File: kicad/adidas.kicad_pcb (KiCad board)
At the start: 2 copper layers, 152.7 x 107.2 mm, 7 parts

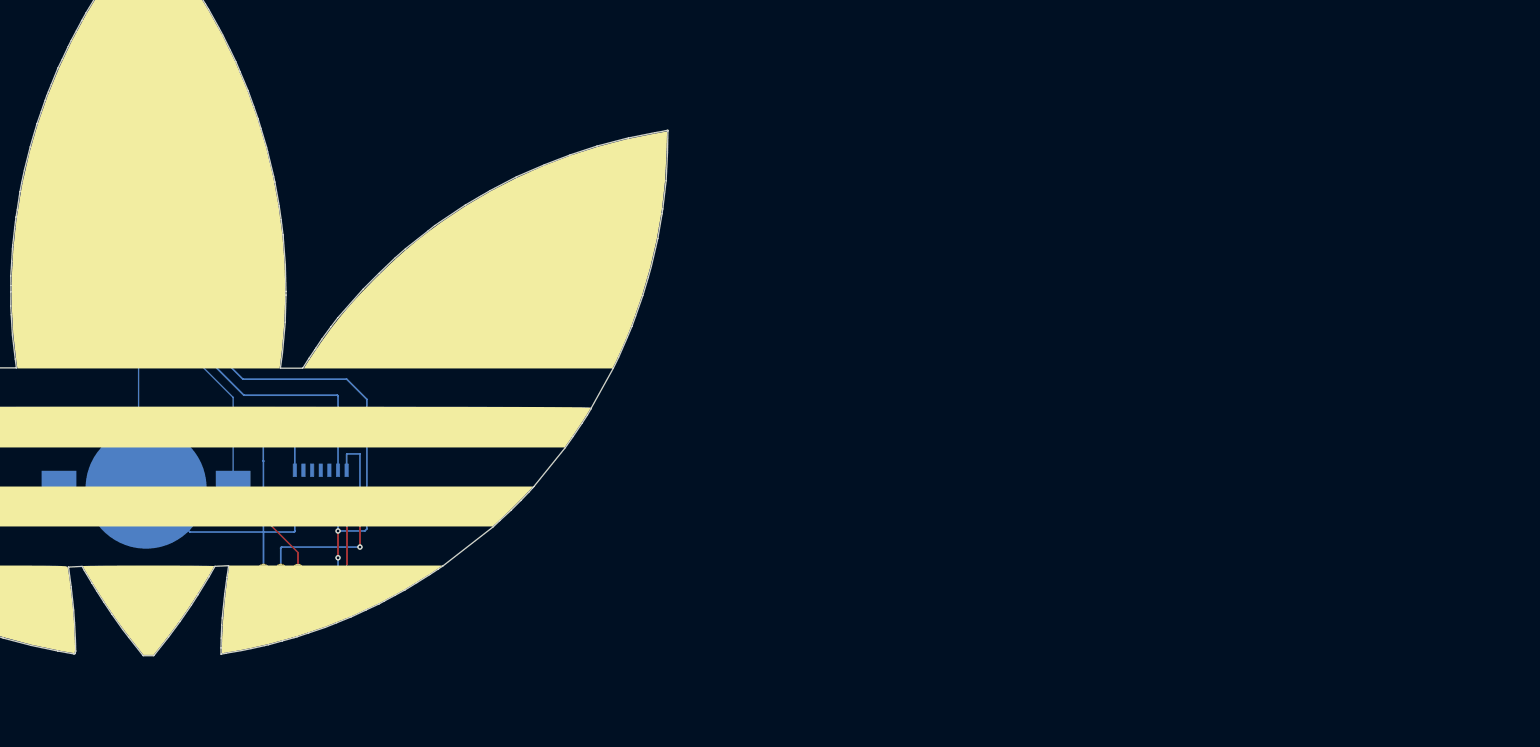
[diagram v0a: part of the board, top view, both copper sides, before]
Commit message: update schematic
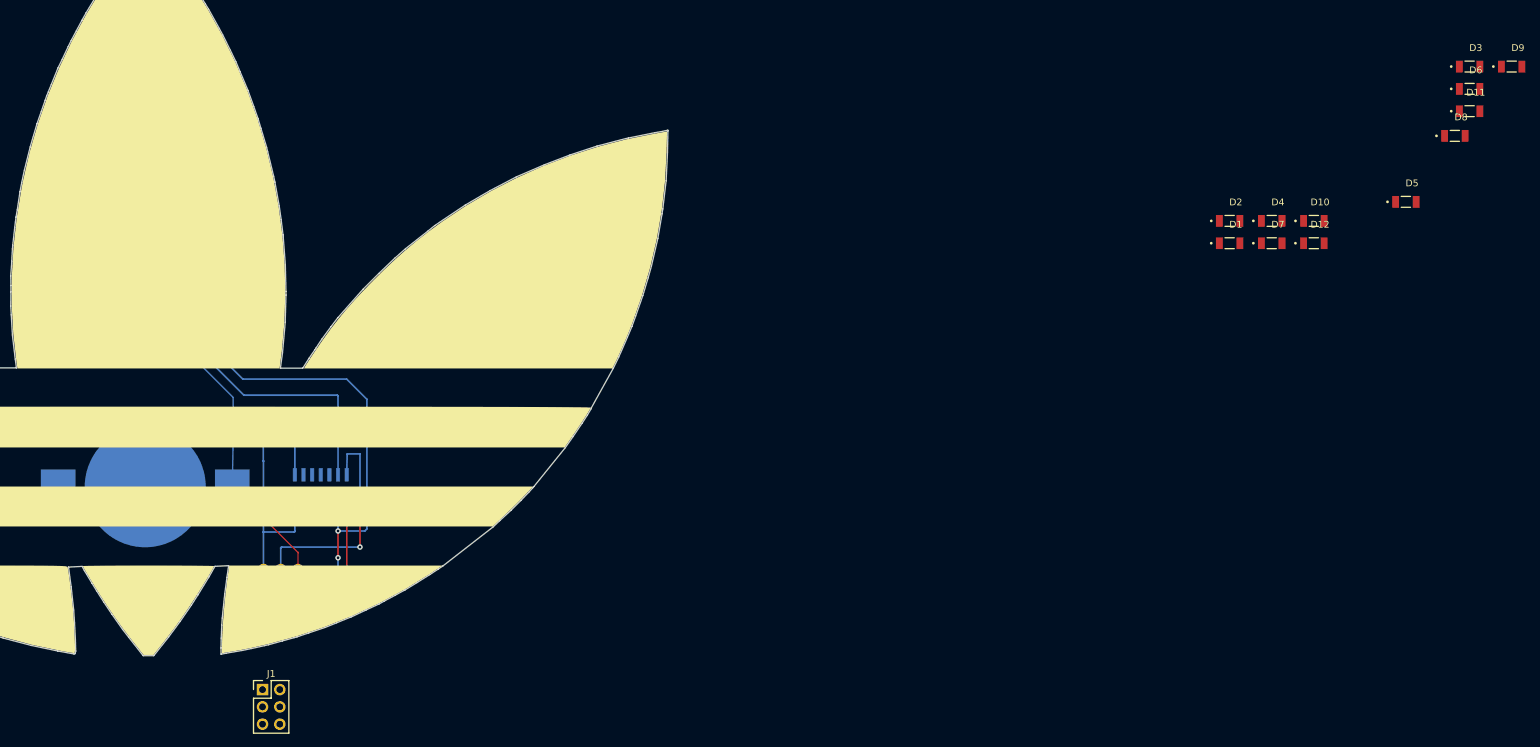
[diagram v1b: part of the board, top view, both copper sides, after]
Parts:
- removed the REF** at (190.4, 120.2)
- removed the REF** at (182.0, 113.3)
- removed the REF** at (164.7, 120.4)
- removed the REF** at (164.9, 99.4)
- added BT1: Battery_Cell, Battery:BatteryHolder_Keystone_3002_1x2032, B.Cu at (164.6, 120.2)
- added D1: LHN974, 1206_smt:LEDC3216X120N, F.Cu at (324.0, 84.4)
- added D10: LHN974, 1206_smt:LEDC3216X120N, F.Cu at (336.4, 81.1)
- added D11: LHN974, 1206_smt:LEDC3216X120N, F.Cu at (359.3, 65.0)
- added D12: LHN974, 1206_smt:LEDC3216X120N, F.Cu at (336.4, 84.4)
- added D2: LHN974, 1206_smt:LEDC3216X120N, F.Cu at (324.0, 81.1)
- added D3: LHN974, 1206_smt:LEDC3216X120N, F.Cu at (359.3, 58.4)
- added D4: LHN974, 1206_smt:LEDC3216X120N, F.Cu at (330.2, 81.1)
- added D5: LHN974, 1206_smt:LEDC3216X120N, F.Cu at (349.9, 78.3)
- added D6: LHN974, 1206_smt:LEDC3216X120N, F.Cu at (359.3, 61.7)
- added D7: LHN974, 1206_smt:LEDC3216X120N, F.Cu at (330.2, 84.4)
- added D8: LHN974, 1206_smt:LEDC3216X120N, F.Cu at (357.1, 68.6)
- added D9: LHN974, 1206_smt:LEDC3216X120N, F.Cu at (365.5, 58.4)
- added J1: Conn_02x03_Odd_Even, Connector_PinHeader_2.54mm:PinHeader_2x03_P2.54mm_Vertical, F.Cu at (181.9, 150.0)
- added J2: Conn_01x02_Female, TestPoint:TestPoint_2Pads_Pitch2.54mm_Drill0.8mm, B.Cu at (182.0, 113.1)
- added U1: MPU-6050, DEAD10C5:QFN50P400X400X95-24N, B.Cu at (167.0, 98.7)
- added U2: ATTINY841-SSU, DEAD10C5:SOIC127P599X175-14N, B.Cu at (190.4, 120.9)
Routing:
- net (no net): track 340.2 -> 0.00 mm, vias 6 -> 1
- net unconnected-(U2-Pad9): track 0.00 -> 102.3 mm, vias 0 -> 1
- net unconnected-(BT1-Pad1): track 0.00 -> 64.5 mm, vias 0 -> 1
- net unconnected-(U2-Pad6): track 0.00 -> 53.9 mm
- net unconnected-(U2-Pad7): track 0.00 -> 34.3 mm, vias 0 -> 2
- net unconnected-(U2-Pad14): track 0.00 -> 27.3 mm
- net unconnected-(U2-Pad8): track 0.00 -> 18.6 mm, vias 0 -> 1
- net unconnected-(BT1-Pad2): track 0.00 -> 1.55 mm

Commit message: add SAO header and place LEDs (#8)
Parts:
- removed the REF** at (187.1, 134.9)
- added J3: SAO Header, Connector_PinHeader_2.54mm:PinHeader_2x03_P2.54mm_Vertical, B.Cu at (162.4, 73.5)
- J1: value Conn_02x03_Odd_Even -> ISP Header; moved to B.Cu
- moved D8 253.1 mm to (106.7, 105.7)
- moved D9 239.4 mm to (130.9, 105.8)
- moved D4 216.8 mm to (116.4, 117.1)
- moved D5 211.3 mm to (142.3, 117.4)
- moved D1 197.6 mm to (131.5, 128.9)
- moved D6 180.0 mm to (188.1, 117.2)
- moved D10 174.4 mm to (163.8, 106.0)
- moved D3 174.3 mm to (200.0, 129.0)
- moved D2 166.2 mm to (164.9, 129.1)
- moved D11 165.2 mm to (199.2, 105.8)
- moved D7 120.8 mm to (214.0, 117.2)
- moved D12 114.7 mm to (223.7, 105.8)
- moved J1 15.6 mm to (187.0, 135.2), turned to 90 degrees
- moved U1 1.92 mm to (165.2, 99.4)
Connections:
- BT1 pad 1: unconnected-(BT1-Pad1) -> +BATT
- BT1 pad 2: unconnected-(BT1-Pad2) -> GND
- D1 pad +: unconnected-(D1-Pad+) -> Net-(D1-Pad+)
- D1 pad -: unconnected-(D1-Pad-) -> GND
- D10 pad +: unconnected-(D10-Pad+) -> Net-(D10-Pad+)
- D10 pad -: unconnected-(D10-Pad-) -> GND
- D11 pad +: unconnected-(D11-Pad+) -> Net-(D10-Pad+)
- D11 pad -: unconnected-(D11-Pad-) -> GND
- D12 pad +: unconnected-(D12-Pad+) -> Net-(D10-Pad+)
- D12 pad -: unconnected-(D12-Pad-) -> GND
- D2 pad +: unconnected-(D2-Pad+) -> Net-(D1-Pad+)
- D2 pad -: unconnected-(D2-Pad-) -> GND
- D3 pad +: unconnected-(D3-Pad+) -> Net-(D1-Pad+)
- D3 pad -: unconnected-(D3-Pad-) -> GND
- D4 pad +: unconnected-(D4-Pad+) -> Net-(D4-Pad+)
- D4 pad -: unconnected-(D4-Pad-) -> GND
- D5 pad +: unconnected-(D5-Pad+) -> Net-(D4-Pad+)
- D5 pad -: unconnected-(D5-Pad-) -> GND
- D6 pad +: unconnected-(D6-Pad+) -> Net-(D4-Pad+)
- D6 pad -: unconnected-(D6-Pad-) -> GND
- D7 pad +: unconnected-(D7-Pad+) -> Net-(D4-Pad+)
- D7 pad -: unconnected-(D7-Pad-) -> GND
- D8 pad +: unconnected-(D8-Pad+) -> Net-(D10-Pad+)
- D8 pad -: unconnected-(D8-Pad-) -> GND
- D9 pad +: unconnected-(D9-Pad+) -> Net-(D10-Pad+)
- D9 pad -: unconnected-(D9-Pad-) -> GND
- J1 pad 1: unconnected-(J1-Pad1) -> Net-(J1-Pad1)
- J1 pad 2: unconnected-(J1-Pad2) -> +BATT
- J1 pad 3: unconnected-(J1-Pad3) -> Net-(J1-Pad3)
- J1 pad 4: unconnected-(J1-Pad4) -> Net-(J1-Pad4)
- J1 pad 6: unconnected-(J1-Pad6) -> GND
- J2 pad 1: unconnected-(J2-Pad1) -> GND
- J2 pad 2: unconnected-(J2-Pad2) -> +BATT
- U1 pad 13: unconnected-(U1-Pad13) -> +BATT
- U1 pad 18: unconnected-(U1-Pad18) -> GND
- U1 pad 23: unconnected-(U1-Pad23) -> Net-(J1-Pad3)
- U1 pad 24: unconnected-(U1-Pad24) -> Net-(J3-Pad3)
- U2 pad 1: unconnected-(U2-Pad1) -> +BATT
- U2 pad 12: unconnected-(U2-Pad12) -> Net-(J3-Pad6)
- U2 pad 13: unconnected-(U2-Pad13) -> Net-(J3-Pad5)
- U2 pad 14: unconnected-(U2-Pad14) -> GND
- U2 pad 2: unconnected-(U2-Pad2) -> Net-(D1-Pad+)
- U2 pad 3: unconnected-(U2-Pad3) -> Net-(D4-Pad+)
- U2 pad 5: unconnected-(U2-Pad5) -> Net-(D10-Pad+)
- U2 pad 6: unconnected-(U2-Pad6) -> Net-(J3-Pad3)
- U2 pad 7: unconnected-(U2-Pad7) -> Net-(J1-Pad4)
- U2 pad 8: unconnected-(U2-Pad8) -> Net-(J1-Pad1)
- U2 pad 9: unconnected-(U2-Pad9) -> Net-(J1-Pad3)
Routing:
- net unconnected-(U2-Pad9): track 102.3 -> 0.00 mm, vias 1 -> 0
- net Net-(J1-Pad3): track 0.00 -> 102.2 mm, vias 0 -> 1
- net GND: track 0.00 -> 68.1 mm
- net unconnected-(BT1-Pad1): track 64.5 -> 0.00 mm, vias 1 -> 0
- net +BATT: track 0.00 -> 61.7 mm, vias 0 -> 1
- net unconnected-(U2-Pad6): track 53.9 -> 0.00 mm
- net Net-(J3-Pad3): track 0.00 -> 53.9 mm
- net Net-(J1-Pad4): track 0.00 -> 34.6 mm, vias 0 -> 2
- net unconnected-(U2-Pad7): track 34.3 -> 0.00 mm, vias 2 -> 0
- net unconnected-(U2-Pad14): track 27.3 -> 0.00 mm
- net unconnected-(U2-Pad8): track 18.6 -> 0.00 mm, vias 1 -> 0
- net Net-(J1-Pad1): track 0.00 -> 18.6 mm, vias 0 -> 1
- net unconnected-(BT1-Pad2): track 1.55 -> 0.00 mm

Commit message: move components
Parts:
- added R1: R, Resistor_SMD:R_1206_3216Metric_Pad1.30x1.75mm_HandSolder, F.Cu at (199.9, 123.1)
- added R2: R, Resistor_SMD:R_1206_3216Metric_Pad1.30x1.75mm_HandSolder, F.Cu at (214.2, 112.4)
- added R3: R, Resistor_SMD:R_1206_3216Metric_Pad1.30x1.75mm_HandSolder, F.Cu at (223.5, 100.3)
- moved J2 80.7 mm to (105.4, 87.7)
- moved J1 75.3 mm to (122.7, 96.1)
- moved U2 45.6 mm to (224.1, 90.1)
- moved BT1 37.2 mm to (165.0, 83.0)
- moved J3 12.7 mm to (162.8, 60.7)
- moved D6 5.08 mm to (183.0, 116.8)
- moved D5 4.70 mm to (147.0, 117.3)
- moved D11 4.45 mm to (194.8, 105.3)
- moved D9 2.04 mm to (132.9, 106.0)
- moved D10 1.79 mm to (165.6, 106.1)
- moved D2 0.61 mm to (165.6, 129.1)
- moved U1 0.34 mm to (165.5, 99.2), turned to 180 degrees
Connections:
- U2 pad 2: Net-(D1-Pad+) -> Net-(U2-Pad2)
- U2 pad 3: Net-(D4-Pad+) -> Net-(U2-Pad3)
- U2 pad 5: Net-(D10-Pad+) -> Net-(U2-Pad5)
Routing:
- net Net-(J1-Pad3): track 102.2 -> 0.04 mm, vias 1 -> 0
- net GND: track 68.1 -> 0.00 mm
- net +BATT: track 61.7 -> 0.04 mm, vias 1 -> 0
- net Net-(J3-Pad3): track 53.9 -> 0.00 mm
- net Net-(J1-Pad4): track 34.6 -> 0.00 mm, vias 2 -> 0
- net Net-(J1-Pad1): track 18.6 -> 0.00 mm, vias 1 -> 0
- net (no net): vias 1 -> 0

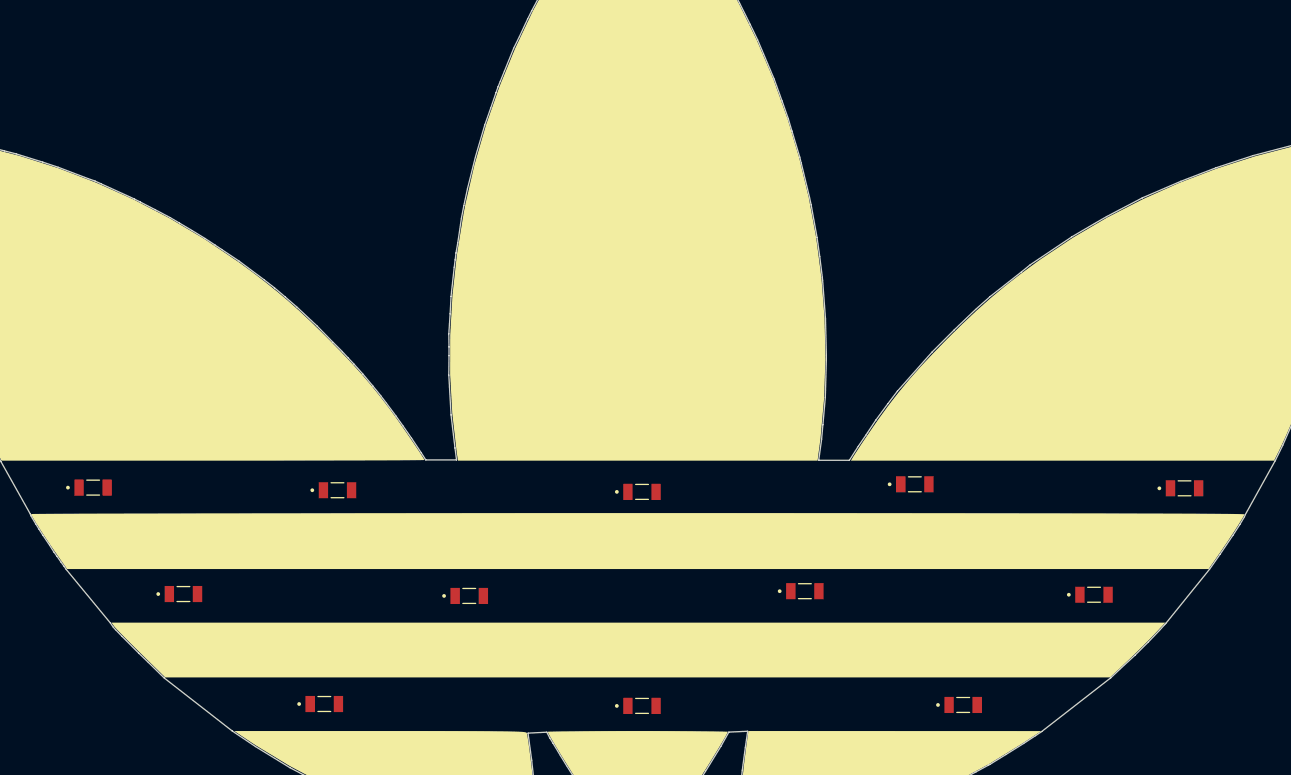
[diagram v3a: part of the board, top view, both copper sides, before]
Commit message: run freeroute on the PCB
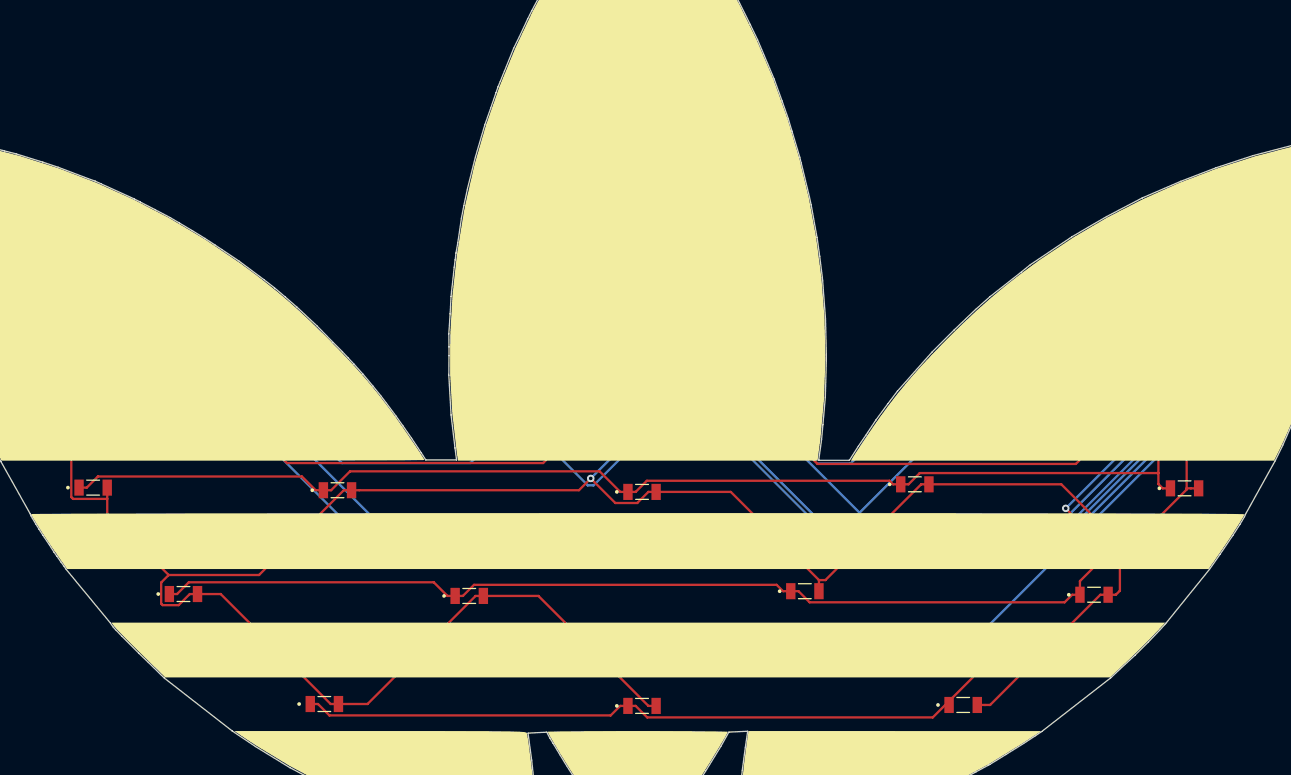
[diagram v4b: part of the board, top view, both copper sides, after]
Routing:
- net GND: track 0.00 -> 334.0 mm, vias 0 -> 2
- net +BATT: track 0.04 -> 222.7 mm
- net Net-(J1-Pad3): track 0.04 -> 192.3 mm, vias 0 -> 1
- net Net-(J1-Pad4): track 0.00 -> 131.9 mm
- net Net-(D10-Pad+): track 0.00 -> 126.6 mm
- net Net-(J3-Pad3): track 0.00 -> 123.4 mm
- net Net-(J1-Pad1): track 0.00 -> 120.5 mm
- net Net-(D4-Pad+): track 0.00 -> 106.4 mm
- net Net-(J3-Pad6): track 0.00 -> 97.1 mm
- net Net-(J3-Pad5): track 0.00 -> 91.7 mm, vias 0 -> 1
- net Net-(D1-Pad+): track 0.00 -> 77.7 mm
- net Net-(U2-Pad2): track 0.00 -> 58.5 mm, vias 0 -> 1
- net Net-(U2-Pad3): track 0.00 -> 31.0 mm, vias 0 -> 1
- net Net-(U2-Pad5): track 0.00 -> 12.8 mm, vias 0 -> 1
